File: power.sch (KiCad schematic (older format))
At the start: 40 parts, among them U1 TPS54325, U2 TPS54294

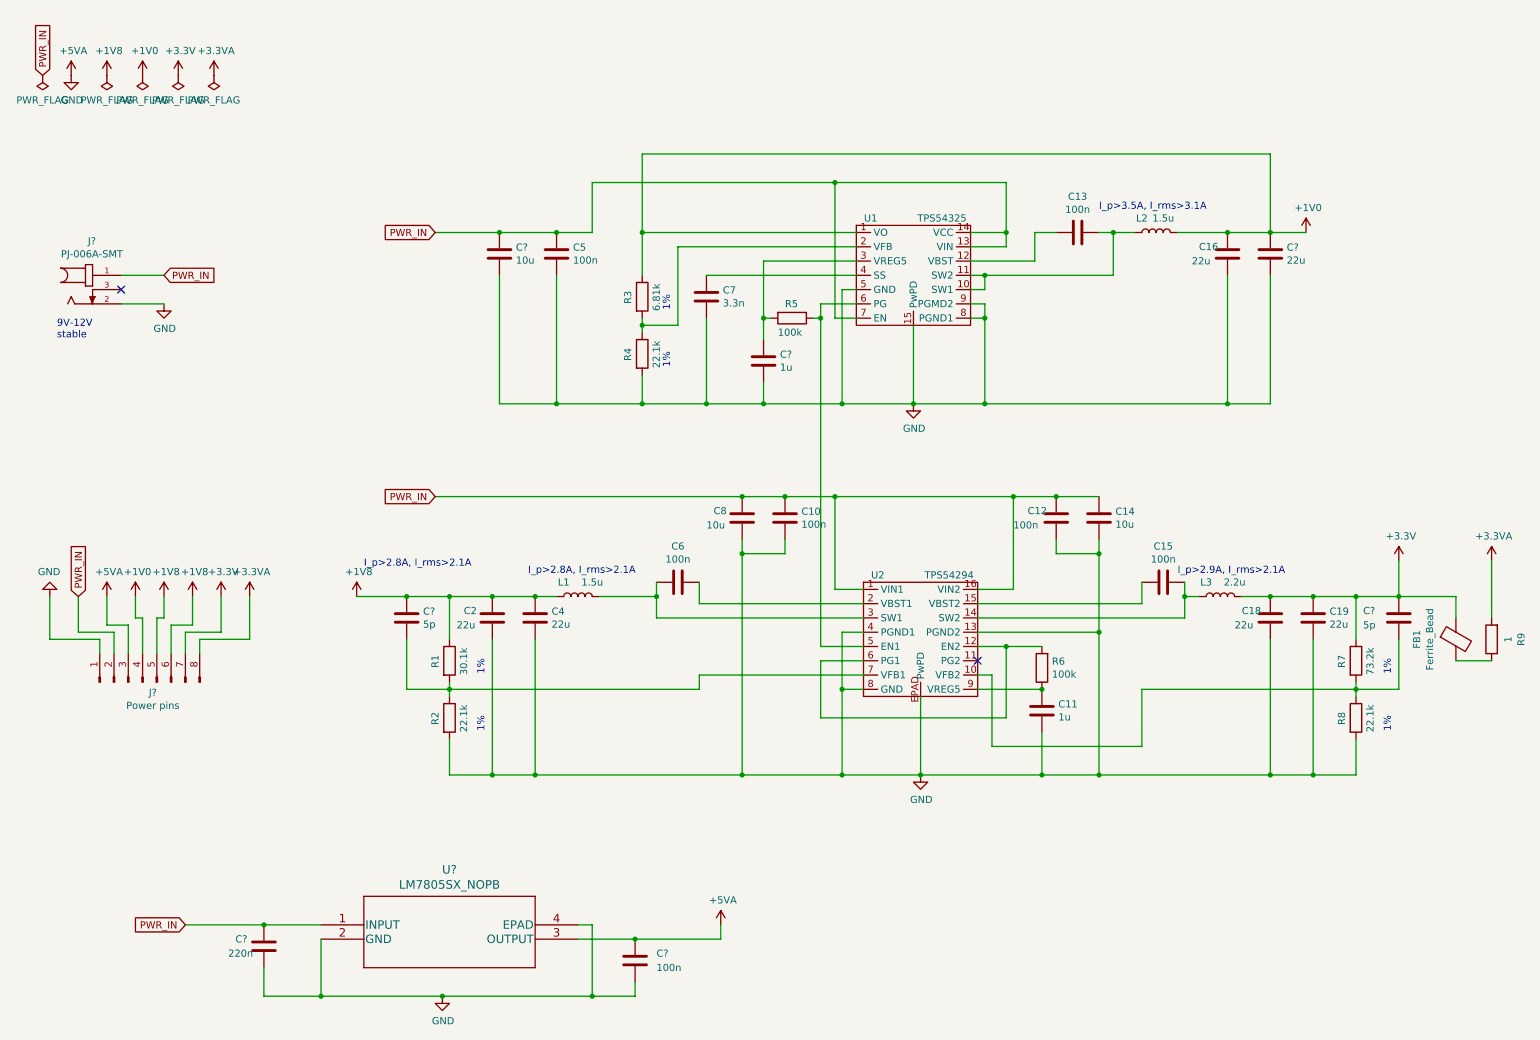
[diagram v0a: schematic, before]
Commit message: Update annotations and footprints
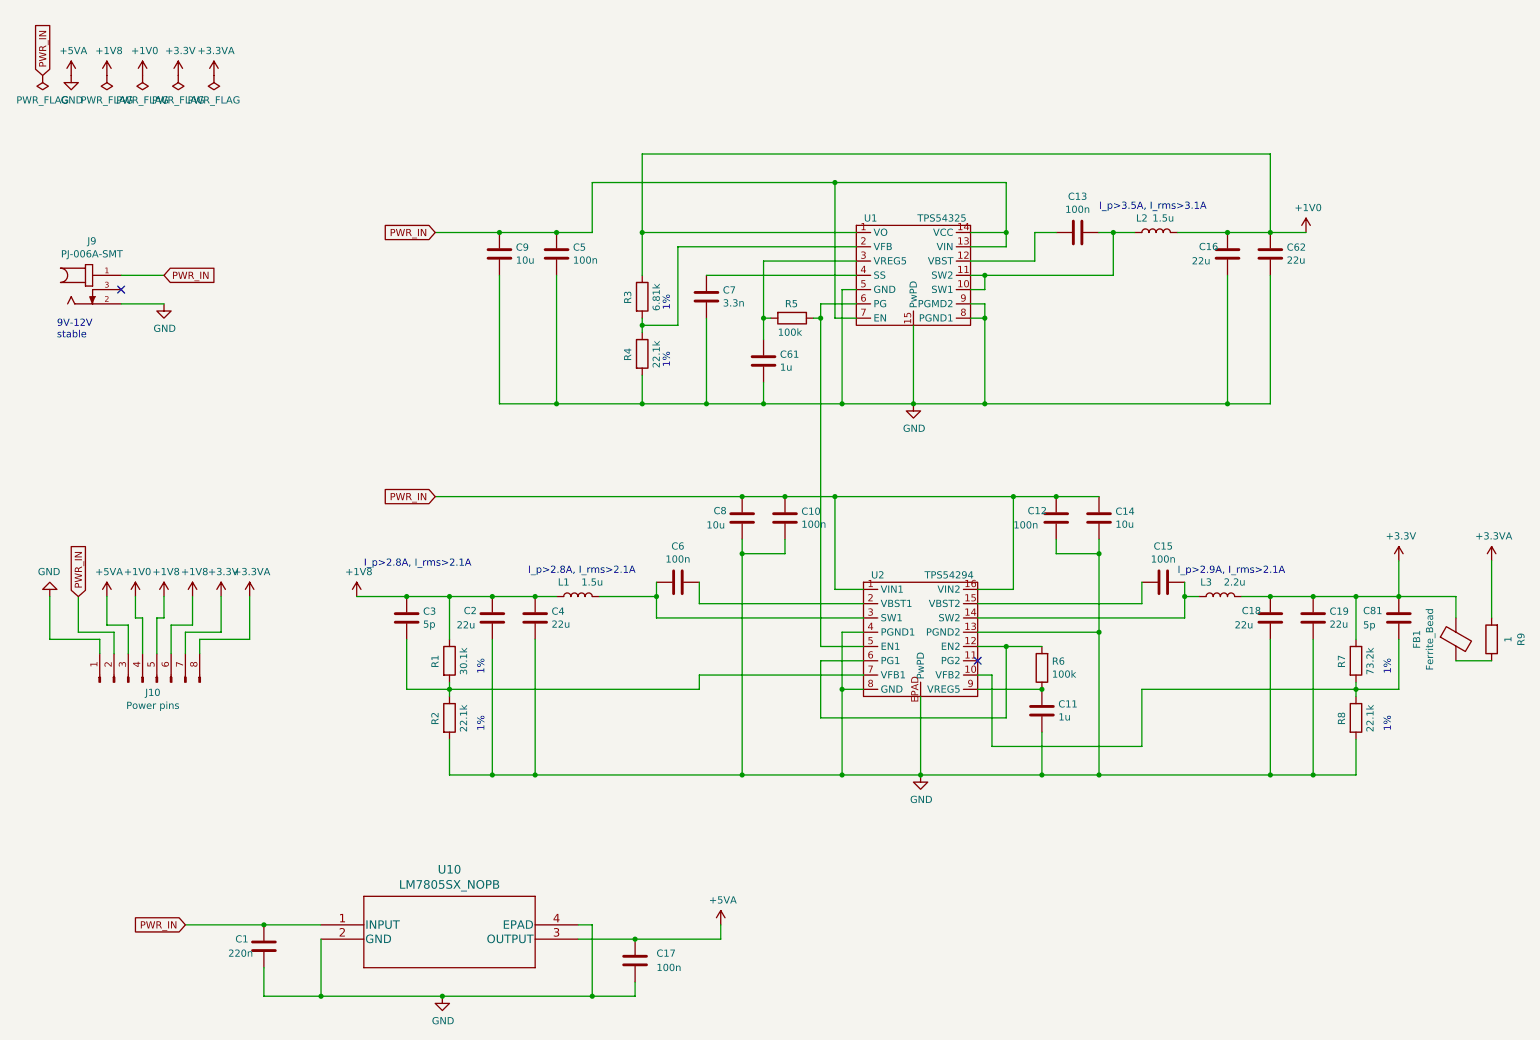
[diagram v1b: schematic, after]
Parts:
- C1, C17, C3, C61, C62, C81, C9: renamed from C?; footprint (none) -> Capacitor_SMD:C_1206_3216Metric_Pad1.42x1.75mm_HandSolder
- C10, C11, C12, C13, C14, C15, C16, C18, C19, C2, C4, C5, C6, C7, C8: footprint (none) -> Capacitor_SMD:C_1206_3216Metric_Pad1.42x1.75mm_HandSolder
- L1, L2, L3: footprint (none) -> VLS5045EX-4R7M:IND_VLS5045EX-4R7M
- R1, R2, R3, R4, R5, R6, R7, R8, R9: footprint (none) -> Resistor_SMD:R_1206_3216Metric_Pad1.42x1.75mm_HandSolder
- gave numbers to parts that had none: 3

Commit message: Organize components and fix minor issues
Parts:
- J10: footprint Connector_PinHeader_1.00mm:PinHeader_1x08_P1.00mm_Vertical -> Connector_PinHeader_2.54mm:PinHeader_1x08_P2.54mm_Vertical
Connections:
- net +5VA: no longer C1.2, C10.2, C11.2, C12.2, C14.2, C16.2, C17.2, C18.2, C19.2, C2.2, C4.2, C5.2, C61.2, C62.2, C7.2, C8.2, C9.2, J10.1 (Pin_1), J9.2, R2.2, R4.2, R8.2, U1.15 (PwPD), U1.5 (GND), U1.8 (PGND1), U1.9 (PGMD2), U10.2 (GND), U10.4 (EPAD), U2.13 (PGND2), U2.4 (PGND1), U2.8 (GND), U2.EPAD (PwPD)
- new net GND: C1.2, C10.2, C11.2, C12.2, C14.2, C16.2, C17.2, C18.2, C19.2, C2.2, C4.2, C5.2, C61.2, C62.2, C7.2, C8.2, C9.2, J10.1 (Pin_1), J9.2, R2.2, R4.2, R8.2, U1.15 (PwPD), U1.5 (GND), U1.8 (PGND1), U1.9 (PGMD2), U10.2 (GND), U10.4 (EPAD), U2.13 (PGND2), U2.4 (PGND1), U2.8 (GND), U2.EPAD (PwPD)
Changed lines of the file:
@@
-$EndComp
-$Comp
-L power:GND #PWR0166
-U 1 1 5D824FDC
-P 950 950
-F 0 "#PWR0166" H 950 700 50  0001 C CNN
-F 1 "GND" H 955 777 50  0000 C CNN
-F 2 "" H 950 950 50  0001 C CNN
-F 3 "" H 950 950 50  0001 C CNN
-	1    950  950
-	1    0    0    -1
 $EndComp
 $Comp
@@
 F 0 "J10" V 1377 5128 50  0000 C CNN
 F 1 "Power pins" V 1286 5128 50  0000 C CNN
-F 2 "Connector_PinHeader_1.00mm:PinHeader_1x08_P1.00mm_Vertical" V 1195 5128 50  0001 C CNN
+F 2 "Connector_PinHeader_2.54mm:PinHeader_1x08_P2.54mm_Vertical" V 1195 5128 50  0001 C CNN
 F 3 "~" H 1450 5200 50  0001 C CNN
 	1    1450 5200
@@
 	1    0    0    -1
 $EndComp
+$Comp
+L power:PWR_FLAG #FLG0102
+U 1 1 5DAB192D
+P 950 950
+F 0 "#FLG0102" H 950 1025 50  0001 C CNN
+F 1 "PWR_FLAG" H 950 1123 50  0000 C CNN
+F 2 "" H 950 950 50  0001 C CNN
+F 3 "~" H 950 950 50  0001 C CNN
+	1    950  950
+	-1   0    0    1
+$EndComp
 $EndSCHEMATC

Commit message: idk
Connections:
- net +1V0: now also J10.5 (Pin_5); no longer J10.4 (Pin_4)
- net +1V8: no longer J10.5 (Pin_5)
- net +5VA: now also J10.4 (Pin_4); no longer J10.3 (Pin_3)
- net GND: now also J10.2 (Pin_2)
- net PWR_IN: now also J10.3 (Pin_3); no longer J10.2 (Pin_2)
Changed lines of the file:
@@
 L power:+1V0 #PWR0171
 U 1 1 5DB55B86
-P 1400 4600
-F 0 "#PWR0171" H 1400 4450 50  0001 C CNN
-F 1 "+1V0" H 1415 4773 50  0000 C CNN
-F 2 "" H 1400 4600 50  0001 C CNN
-F 3 "" H 1400 4600 50  0001 C CNN
-	1    1400 4600
-	1    0    0    -1
-$EndComp
-$Comp
-L power:+1V8 #PWR0172
-U 1 1 5DB5DE90
 P 1600 4600
-F 0 "#PWR0172" H 1600 4450 50  0001 C CNN
-F 1 "+1V8" H 1615 4773 50  0000 C CNN
+F 0 "#PWR0171" H 1600 4450 50  0001 C CNN
+F 1 "+1V0" H 1615 4773 50  0000 C CNN
 F 2 "" H 1600 4600 50  0001 C CNN
 F 3 "" H 1600 4600 50  0001 C CNN
@@
 Text GLabel 3500 3900 0    50   Input ~ 0
 PWR_IN
-Text GLabel 1000 4600 1    50   Input ~ 0
+Text GLabel 1200 4600 1    50   Input ~ 0
 PWR_IN
 $Comp
 L power:+5VA #PWR0177
 U 1 1 5D9E5717
-P 1200 4600
-F 0 "#PWR0177" H 1200 4450 50  0001 C CNN
-F 1 "+5VA" H 1215 4773 50  0000 C CNN
-F 2 "" H 1200 4600 50  0001 C CNN
-F 3 "" H 1200 4600 50  0001 C CNN
-	1    1200 4600
+P 1400 4600
+F 0 "#PWR0177" H 1400 4450 50  0001 C CNN
+F 1 "+5VA" H 1415 4773 50  0000 C CNN
+F 2 "" H 1400 4600 50  0001 C CNN
+F 3 "" H 1400 4600 50  0001 C CNN
+	1    1400 4600
 	1    0    0    -1
 $EndComp
@@
 	-1   0    0    1
 $EndComp
+$Comp
+L power:GND #PWR?
+U 1 1 5D90CAF6
+P 1000 4600
+F 0 "#PWR?" H 1000 4350 50  0001 C CNN
+F 1 "GND" H 1005 4427 50  0000 C CNN
+F 2 "" H 1000 4600 50  0001 C CNN
+F 3 "" H 1000 4600 50  0001 C CNN
+	1    1000 4600
+	-1   0    0    1
+$EndComp

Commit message: Route PSU
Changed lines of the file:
@@
 	1    0    0    -1
 $EndComp
-Text Notes 3000 4400 0    50   ~ 0
-I_p>2.8A, I_rms>2.1A
 $Comp
 L Device:C C2
